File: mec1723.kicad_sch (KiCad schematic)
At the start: 87 parts, among them J3001 PinHeader_2x5_P1.27mm_SMD, J3002 PinHeader_2x5_P1.27mm_SMD, J3003 PinHeader_2x5_P1.27mm_SMD, J3004 PinHeader_2x5_P1.27mm_SMD, J3005 PinHeader_2x5_P1.27mm_SMD, J3006 PinHeader_2x5_P1.27mm_SMD, J3007 PinHeader_2x5_P1.27mm_SMD, J3008 PinHeader_2x5_P1.27mm_SMD, J3009 PinHeader_2x5_P1.27mm_SMD, J3010 PinHeader_2x5_P1.27mm_SMD, J3011 PinHeader_2x5_P1.27mm_SMD, SW3001 SW_KSC441J70SHLFS_SMD, SW3002 SW_KSC441J70SHLFS_SMD, SW3004 SW_KSC441J70SHLFS_SMD, U3001 MEC1723N-B0-I/SZ, Y3001 Resonator_32.768kHz_ECX-31B

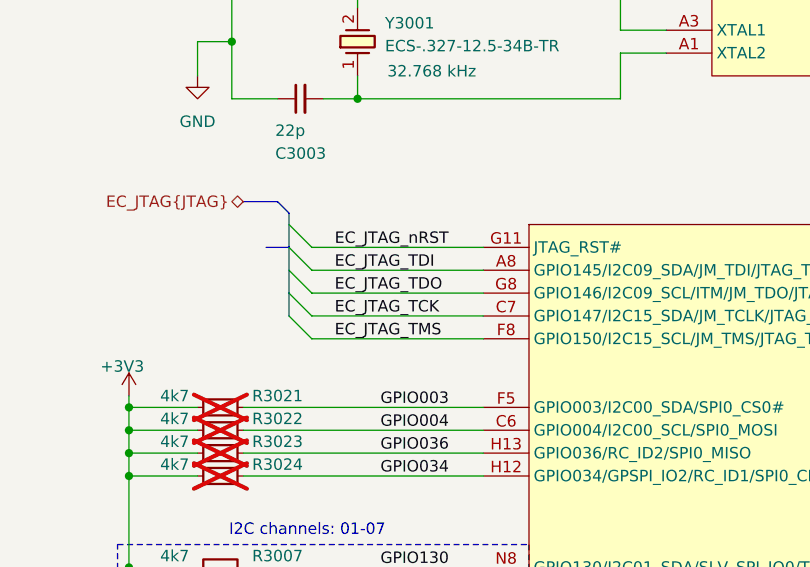
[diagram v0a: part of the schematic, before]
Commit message: [#103697] Route qSPI, 7seg, and 1V8 plane, fix issues
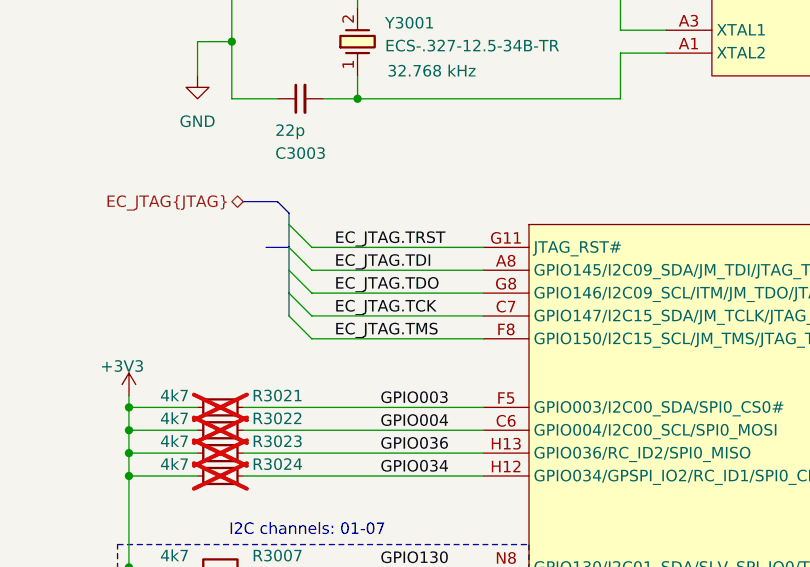
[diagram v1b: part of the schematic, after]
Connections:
- net EC_JTAG_TCK renamed EC_JTAG.TCK
- net EC_JTAG_TDI renamed EC_JTAG.TDI
- net EC_JTAG_TDO renamed EC_JTAG.TDO
- net EC_JTAG_TMS renamed EC_JTAG.TMS
- net EC_JTAG_nRST renamed EC_JTAG.TRST
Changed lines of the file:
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@@
 		)
 	)
-	(label "EC_JTAG_TDO"
+	(label "EC_JTAG.TDO"
 		(at 139.7 111.76 0)
 		(effects
@@
 		)
 	)
-	(label "EC_JTAG_TMS"
+	(label "EC_JTAG.TMS"
 		(at 139.7 116.84 0)
 		(effects
@@
 		)
 	)
-	(label "EC_JTAG_nRST"
+	(label "EC_JTAG.TRST"
 		(at 139.7 106.68 0)
 		(effects
@@
 		)
 	)
-	(label "EC_JTAG_TCK"
+	(label "EC_JTAG.TCK"
 		(at 139.7 114.3 0)
 		(effects
@@
 		)
 	)
-	(label "EC_JTAG_TDI"
+	(label "EC_JTAG.TDI"
 		(at 139.7 109.22 0)
 		(effects

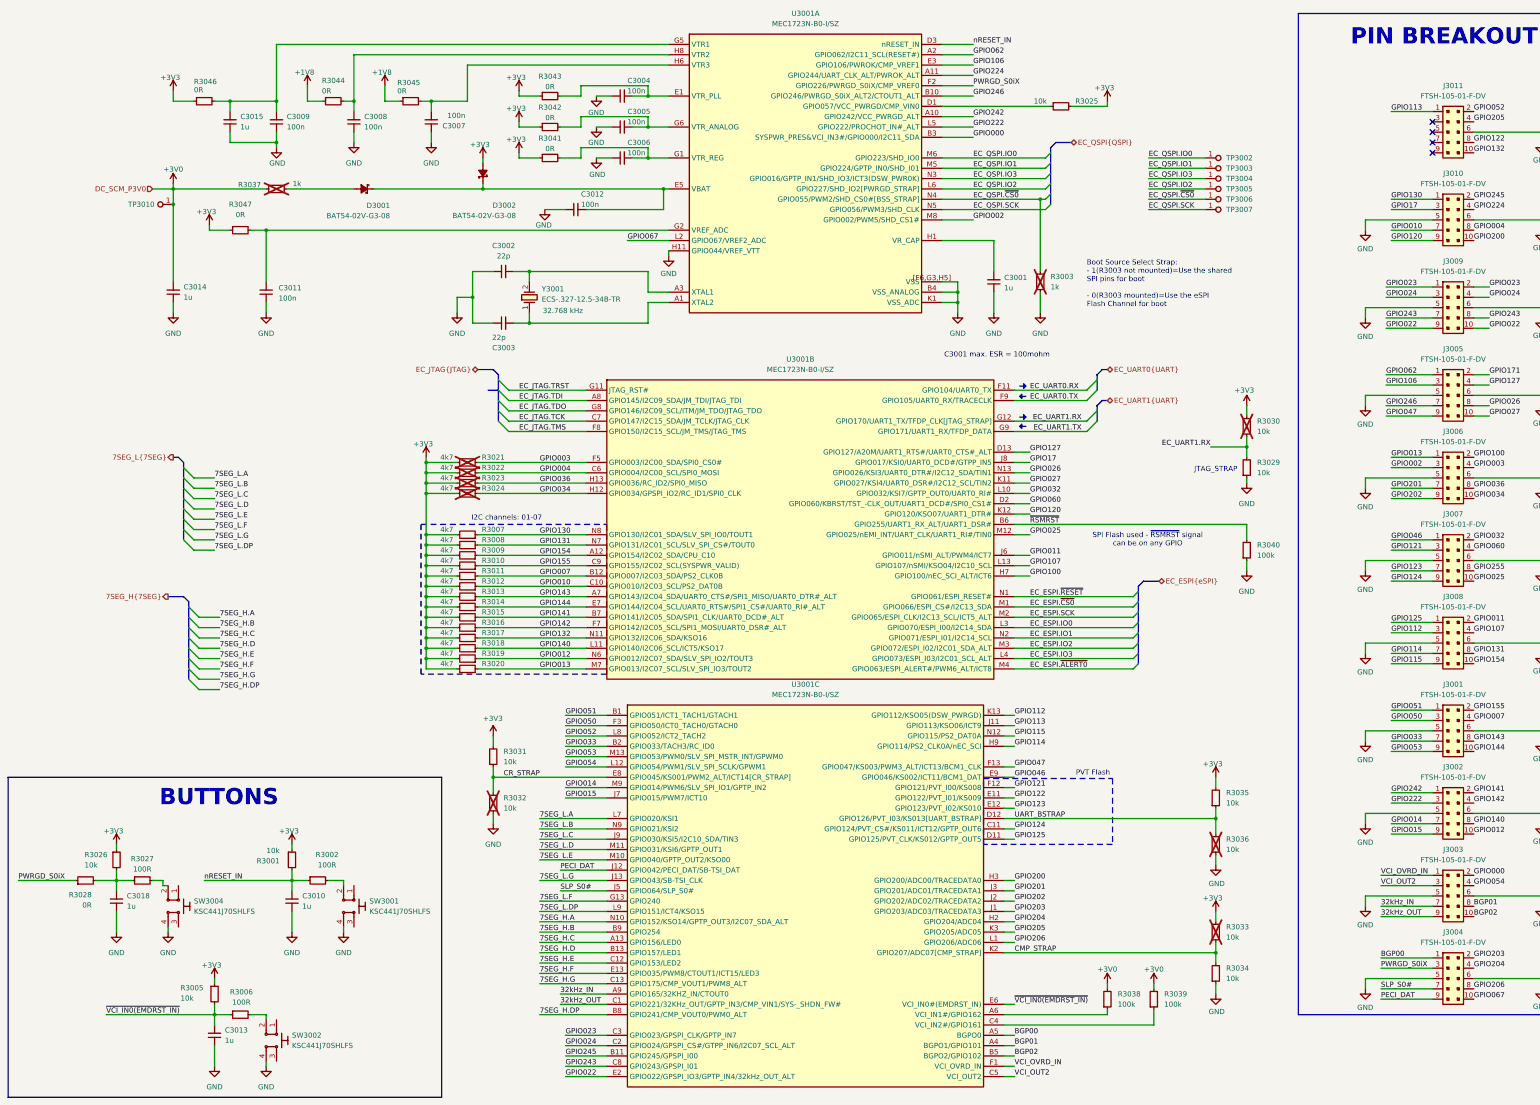
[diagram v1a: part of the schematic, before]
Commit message: [#103697] Reenumerate the entire schematic, rerouting eSPI to maintain bigger gap between traces, rerouting the LDO
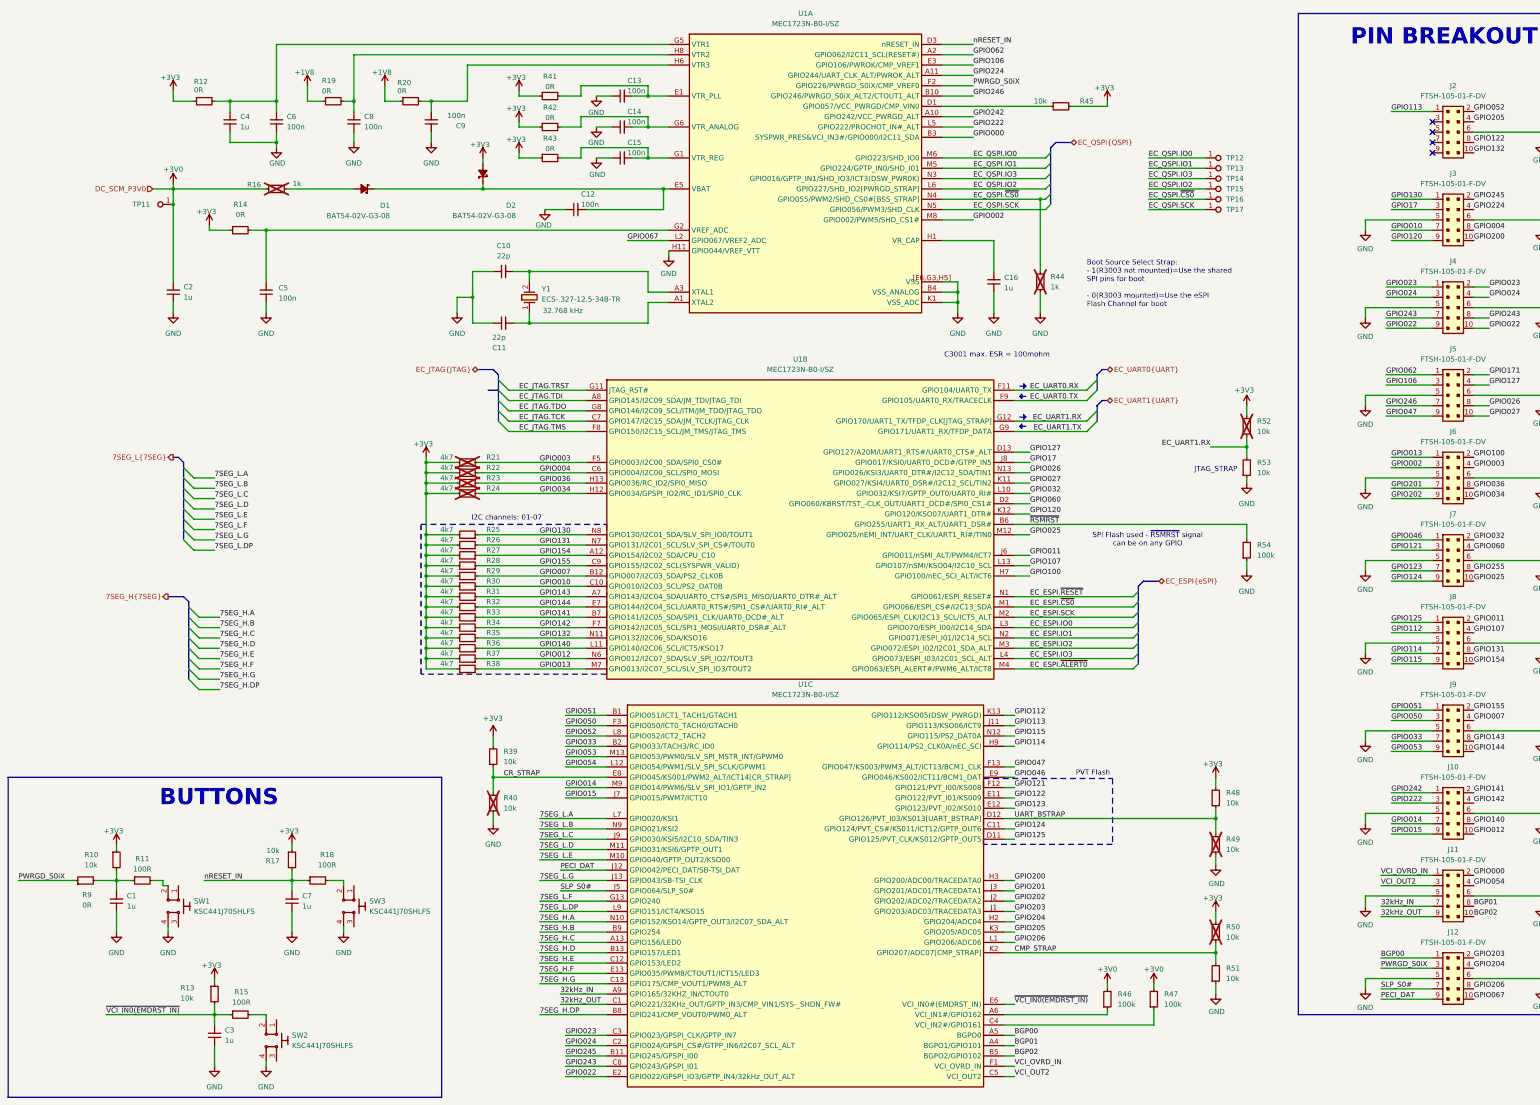
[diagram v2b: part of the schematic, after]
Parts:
- renumbered C3018 to C1, C3002 to C10, C3003 to C11, C3012 to C12, C3004 to C13, C3005 to C14, C3006 to C15, C3001 to C16, C3014 to C2, C3013 to C3, C3015 to C4, C3011 to C5, C3009 to C6, C3010 to C7, C3008 to C8, C3007 to C9, D3001 to D1, D3002 to D2, J3002 to J10, J3003 to J11, J3004 to J12, J3011 to J2, J3010 to J3, J3009 to J4, J3005 to J5, J3006 to J6, J3007 to J7, J3008 to J8, J3001 to J9, R3026 to R10, R3027 to R11, R3046 to R12, R3005 to R13, R3047 to R14, R3006 to R15, R3037 to R16, R3001 to R17, R3002 to R18, R3044 to R19, R3045 to R20, R3021 to R21, R3022 to R22, R3023 to R23, R3024 to R24, R3007 to R25, R3008 to R26, R3009 to R27, R3010 to R28, R3011 to R29, R3012 to R30, R3013 to R31, R3014 to R32, R3015 to R33, R3016 to R34, R3017 to R35, R3018 to R36, R3019 to R37, R3020 to R38, R3031 to R39, R3032 to R40, R3043 to R41, R3042 to R42, R3041 to R43, R3003 to R44, R3025 to R45, R3038 to R46, R3039 to R47, R3035 to R48, R3036 to R49, R3033 to R50, R3034 to R51, R3030 to R52, R3029 to R53, R3040 to R54, R3028 to R9, SW3004 to SW1, SW3002 to SW2, SW3001 to SW3, TP3010 to TP11, TP3002 to TP12, TP3003 to TP13, TP3004 to TP14, TP3005 to TP15, TP3006 to TP16, TP3007 to TP17, U3001 to U1, Y3001 to Y1

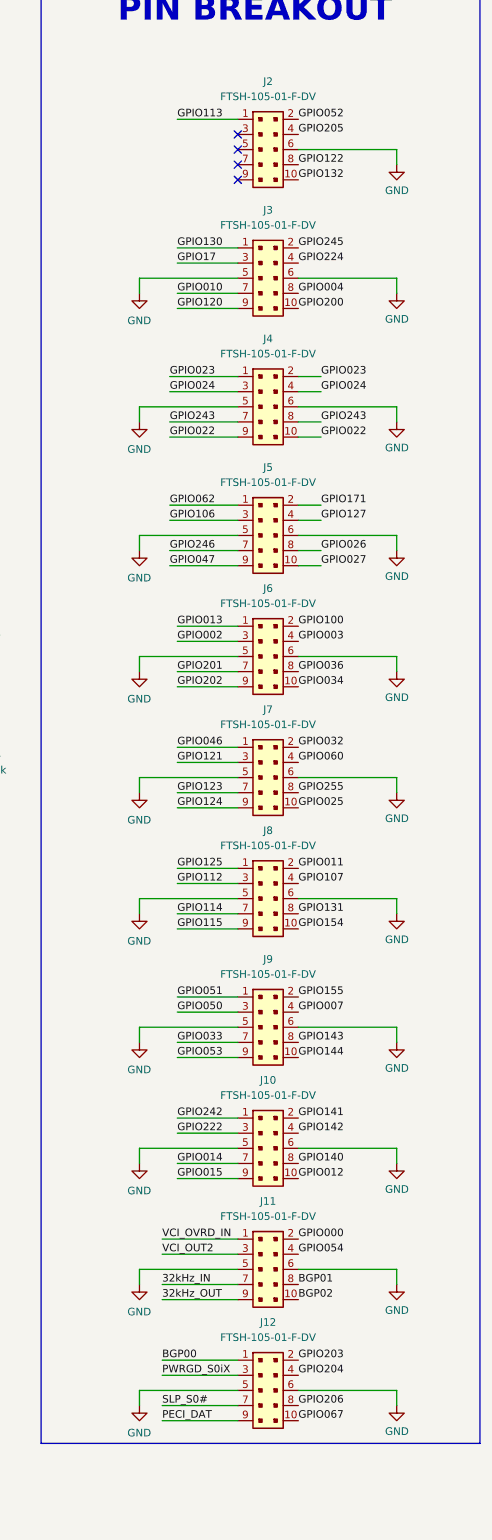
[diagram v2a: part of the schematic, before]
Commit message: [#103697] sch: mec1723: set J2-J12 as DNP
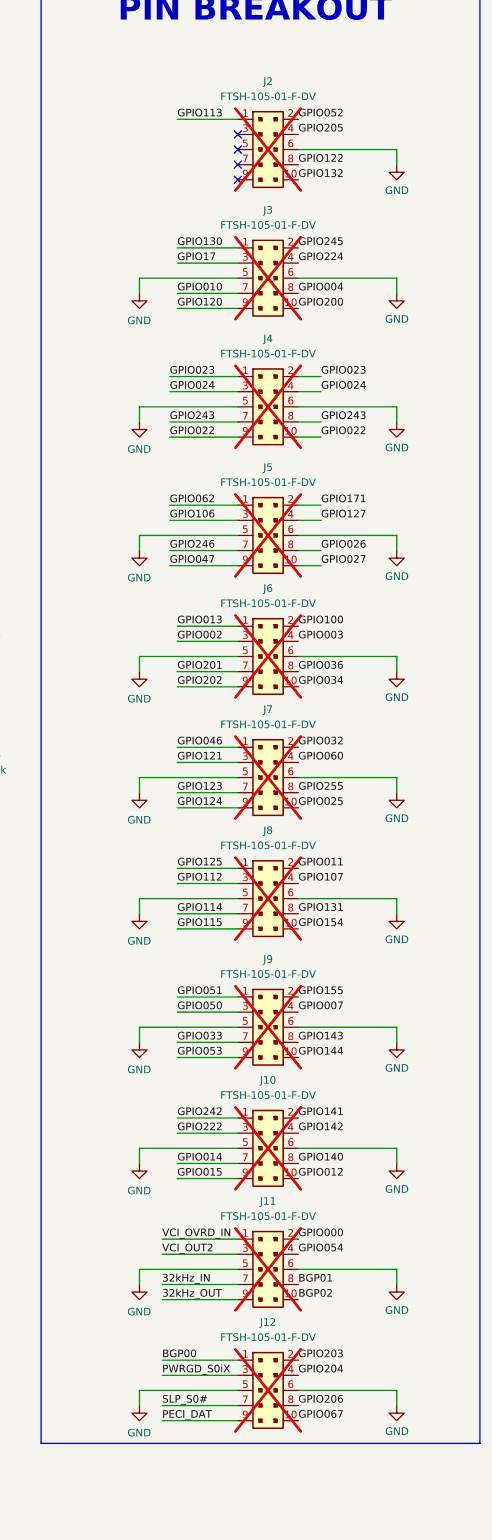
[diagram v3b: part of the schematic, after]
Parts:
- J10, J11, J12, J2, J3, J4, J5, J6, J7, J8, J9: now not fitted
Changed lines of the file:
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@@
 		(on_board yes)
 		(in_pos_files yes)
-		(dnp no)
+		(dnp yes)
 		(fields_autoplaced yes)
 		(property "Reference" "J10"
@@
 		(on_board yes)
 		(in_pos_files yes)
-		(dnp no)
+		(dnp yes)
 		(fields_autoplaced yes)
 		(property "Reference" "J9"
@@
 		(on_board yes)
 		(in_pos_files yes)
-		(dnp no)
+		(dnp yes)
 		(fields_autoplaced yes)
 		(property "Reference" "J5"
@@
 		(on_board yes)
 		(in_pos_files yes)
-		(dnp no)
+		(dnp yes)
 		(fields_autoplaced yes)
 		(property "Reference" "J8"
@@
 		(on_board yes)
 		(in_pos_files yes)
-		(dnp no)
+		(dnp yes)
 		(fields_autoplaced yes)
 		(property "Reference" "J6"
@@
 		(on_board yes)
 		(in_pos_files yes)
-		(dnp no)
+		(dnp yes)
 		(fields_autoplaced yes)
 		(property "Reference" "J2"
@@
 		(on_board yes)
 		(in_pos_files yes)
-		(dnp no)
+		(dnp yes)
 		(fields_autoplaced yes)
 		(property "Reference" "J4"
@@
 		(on_board yes)
 		(in_pos_files yes)
-		(dnp no)
+		(dnp yes)
 		(fields_autoplaced yes)
 		(property "Reference" "J3"
@@
 		(on_board yes)
 		(in_pos_files yes)
-		(dnp no)
+		(dnp yes)
 		(fields_autoplaced yes)
 		(property "Reference" "J12"
@@
 		(on_board yes)
 		(in_pos_files yes)
-		(dnp no)
+		(dnp yes)
 		(fields_autoplaced yes)
 		(property "Reference" "J7"
@@
 		(on_board yes)
 		(in_pos_files yes)
-		(dnp no)
+		(dnp yes)
 		(fields_autoplaced yes)
 		(property "Reference" "J11"

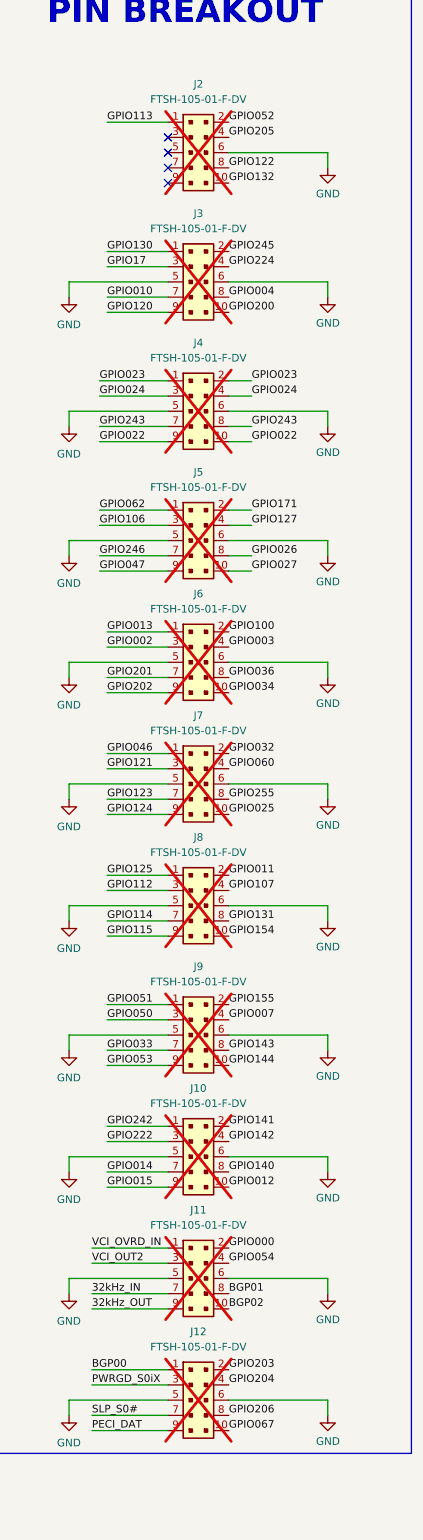
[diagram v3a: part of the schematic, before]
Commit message: [#103697] Fix decoupling nets, route JTAG, buttons, UART, power
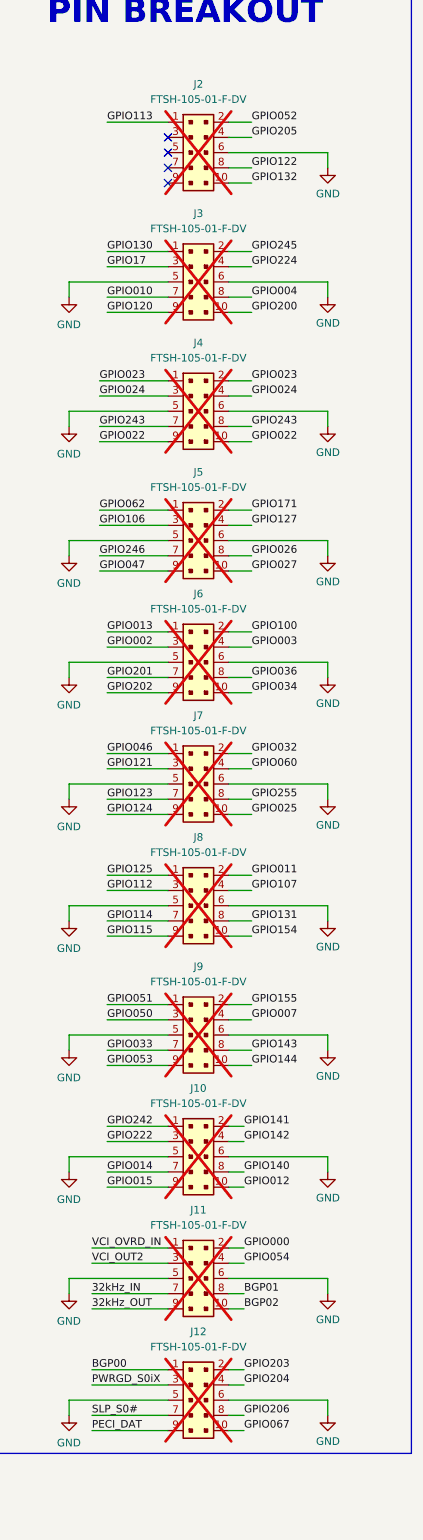
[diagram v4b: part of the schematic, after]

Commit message: [#103697] Route 7seg, fix power rails, leaving GPIO disconnected
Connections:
- net 7SEG_H.A: now also U1.D2 (GPIO060/KBRST/TST_-CLK_OUT/UART1_DCD#/SPI0_CS1#); no longer U1.N10 (GPIO152/KSO14/GPTP_OUT3/I2C07_SDA_ALT)
- net 7SEG_H.B: now also U1.C2 (GPIO024/GPSPI_CS#/GTPP_IN6/I2C07_SCL_ALT); no longer U1.B9 (GPIO254)
- net 7SEG_H.C: now also U1.B1 (GPIO051/ICT1_TACH1/GTACH1); no longer U1.A13 (GPIO156/LED0)
- net 7SEG_H.D: now also U1.B2 (GPIO033/TACH3/RC_ID0); no longer U1.B13 (GPIO157/LED1)
- net 7SEG_H.DP: now also U1.C3 (GPIO023/GPSPI_CLK/GPTP_IN7); no longer U1.B8 (GPIO241/CMP_VOUT0/PWM0_ALT)
- net 7SEG_H.E: now also U1.F3 (GPIO050/ICT0_TACH0/GTACH0); no longer U1.C12 (GPIO153/LED2)
- net 7SEG_H.F: now also U1.E3 (GPIO106/PWROK/CMP_VREF1); no longer U1.E13 (GPIO035/PWM8/CTOUT1/ICT15/LED3)
- net 7SEG_H.G: now also U1.A2 (GPIO062/I2C11_SCL(RESET#)); no longer U1.C13 (GPIO175/CMP_VOUT1/PWM8_ALT)
- net 7SEG_L.A: now also U1.L1 (GPIO206/ADC06); no longer U1.L7 (GPIO020/KSI1)
- net 7SEG_L.B: now also U1.L2 (GPIO067/VREF2_ADC); no longer U1.N9 (GPIO021/KSI2)
- net 7SEG_L.C: now also U1.J1 (GPIO203/ADC03/TRACEDATA3); no longer U1.J9 (GPIO030/KSI5/I2C10_SDA/TIN3)
- net 7SEG_L.D: now also U1.K3 (GPIO205/ADC05); no longer U1.M11 (GPIO031/KSI6/GPTP_OUT1)
- net 7SEG_L.DP: now also U1.H3 (GPIO200/ADC00/TRACEDATA0); no longer U1.L9 (GPIO151/ICT4/KSO15)
- net 7SEG_L.E: now also U1.J2 (GPIO202/ADC02/TRACEDATA2); no longer U1.M10 (GPIO040/GPTP_OUT2/KSO00)
- net 7SEG_L.F: now also U1.H2 (GPIO204/ADC04); no longer U1.G13 (GPIO240)
- net 7SEG_L.G: now also U1.J3 (GPIO201/ADC01/TRACEDATA1); no longer U1.J13 (GPIO043/SB-TSI_CLK)
- net GPIO000: no longer J11.2
- net GPIO002: no longer J6.3
- net GPIO003: no longer J6.4
- net GPIO004: no longer J3.8
- net GPIO007: no longer J9.4
- net GPIO010: no longer J3.7
- net GPIO011: no longer J8.2
- net GPIO012: no longer J10.10
- net GPIO013: no longer J6.1
- net GPIO014: no longer J10.7
- net GPIO015: no longer J10.9
- net GPIO022: no longer J4.10, J4.9
- net GPIO023: no longer J4.1, J4.2, U1.C3 (GPIO023/GPSPI_CLK/GPTP_IN7)
- net GPIO025: no longer J7.10
- net GPIO026: no longer J5.8, U1.N13 (GPIO026/KSI3/UART0_DTR#/I2C12_SDA/TIN1)
- net GPIO027: no longer J5.10
- net GPIO032: no longer J7.2
- net GPIO034: no longer J6.10
- net GPIO036: no longer J6.8
- net GPIO046: no longer J7.1
- net GPIO047: no longer J5.9
- net GPIO052: no longer J2.2
- net GPIO053: no longer J9.9
- net GPIO054: no longer J11.4
- net GPIO067: no longer J12.10, U1.L2 (GPIO067/VREF2_ADC)
- net GPIO100: no longer J6.2
- net GPIO107: no longer J8.4
- net GPIO112: no longer J8.3
- net GPIO113: no longer J2.1
- net GPIO114: no longer J8.7
- net GPIO115: no longer J8.9
- net GPIO120: no longer J3.9
- net GPIO121: no longer J7.3
- net GPIO122: no longer J2.8
- net GPIO123: no longer J7.7
- net GPIO124: no longer J7.9
- net GPIO125: no longer J8.1
- net GPIO127: no longer J5.4
- net GPIO130: no longer J3.1
- net GPIO131: no longer J8.8
- net GPIO132: no longer J2.10
- net GPIO140: no longer J10.8
- net GPIO141: no longer J10.2
- net GPIO142: no longer J10.4
- net GPIO143: no longer J9.8
- net GPIO144: no longer J9.10
- net GPIO154: no longer J8.10
- net GPIO155: no longer J9.2
- net GPIO17: no longer J3.3
- net GPIO171: no longer J5.2
- net GPIO203: no longer J12.2, U1.J1 (GPIO203/ADC03/TRACEDATA3)
- net GPIO205: no longer J2.4, U1.K3 (GPIO205/ADC05)
- net GPIO206: no longer J12.8, U1.L1 (GPIO206/ADC06)
- net GPIO222: no longer J10.3
- net GPIO224: no longer J3.4
- net GPIO242: no longer J10.1
- net GPIO243: no longer J4.7, J4.8
- net GPIO245: no longer J3.2
- net GPIO246: no longer J5.7
- net GPIO255: no longer J7.8
- removed net GPIO024: J4.3, J4.4, U1.C2 (GPIO024/GPSPI_CS#/GTPP_IN6/I2C07_SCL_ALT)
- net GPIO033: no longer names the net of J9.7
- net GPIO033: no longer U1.B2 (GPIO033/TACH3/RC_ID0)
- net GPIO050: no longer names the net of J9.3
- net GPIO050: no longer U1.F3 (GPIO050/ICT0_TACH0/GTACH0)
- net GPIO051: no longer names the net of J9.1
- net GPIO051: no longer U1.B1 (GPIO051/ICT1_TACH1/GTACH1)
- net GPIO060: no longer names the net of J7.4
- net GPIO060: no longer U1.D2 (GPIO060/KBRST/TST_-CLK_OUT/UART1_DCD#/SPI0_CS1#)
- net GPIO062: no longer names the net of J5.1
- net GPIO062: no longer U1.A2 (GPIO062/I2C11_SCL(RESET#))
- net GPIO106: no longer names the net of J5.3
- net GPIO106: no longer U1.E3 (GPIO106/PWROK/CMP_VREF1)
- net GPIO200: no longer names the net of J3.10
- net GPIO200: no longer U1.H3 (GPIO200/ADC00/TRACEDATA0)
- net GPIO201: no longer names the net of J6.7
- net GPIO201: no longer U1.J3 (GPIO201/ADC01/TRACEDATA1)
- net GPIO202: no longer names the net of J6.9
- net GPIO202: no longer U1.J2 (GPIO202/ADC02/TRACEDATA2)
- net GPIO204: no longer names the net of J12.4
- net GPIO204: no longer U1.H2 (GPIO204/ADC04)
- new net GPIO020: U1.L7 (GPIO020/KSI1)
- new net GPIO021: U1.N9 (GPIO021/KSI2)
- new net GPIO030: U1.J9 (GPIO030/KSI5/I2C10_SDA/TIN3)
- new net GPIO031: U1.M11 (GPIO031/KSI6/GPTP_OUT1)
- new net GPIO040: U1.M10 (GPIO040/GPTP_OUT2/KSO00)
- new net GPIO043: U1.G13 (GPIO240), U1.J13 (GPIO043/SB-TSI_CLK)
- no-connect marks 4 -> 0
